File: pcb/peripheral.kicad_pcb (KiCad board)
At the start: 2 copper layers, 37 x 19.6 mm, 0 parts

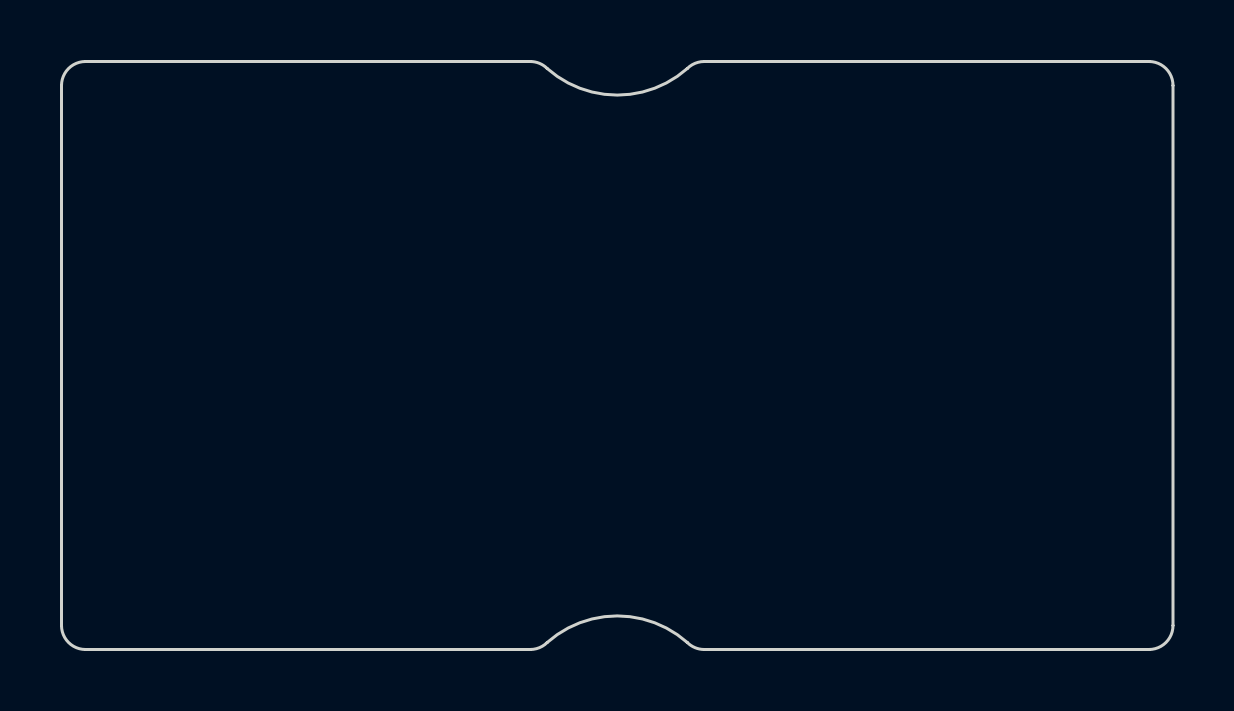
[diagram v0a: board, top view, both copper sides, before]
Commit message: Add Molex connector to peripheral template
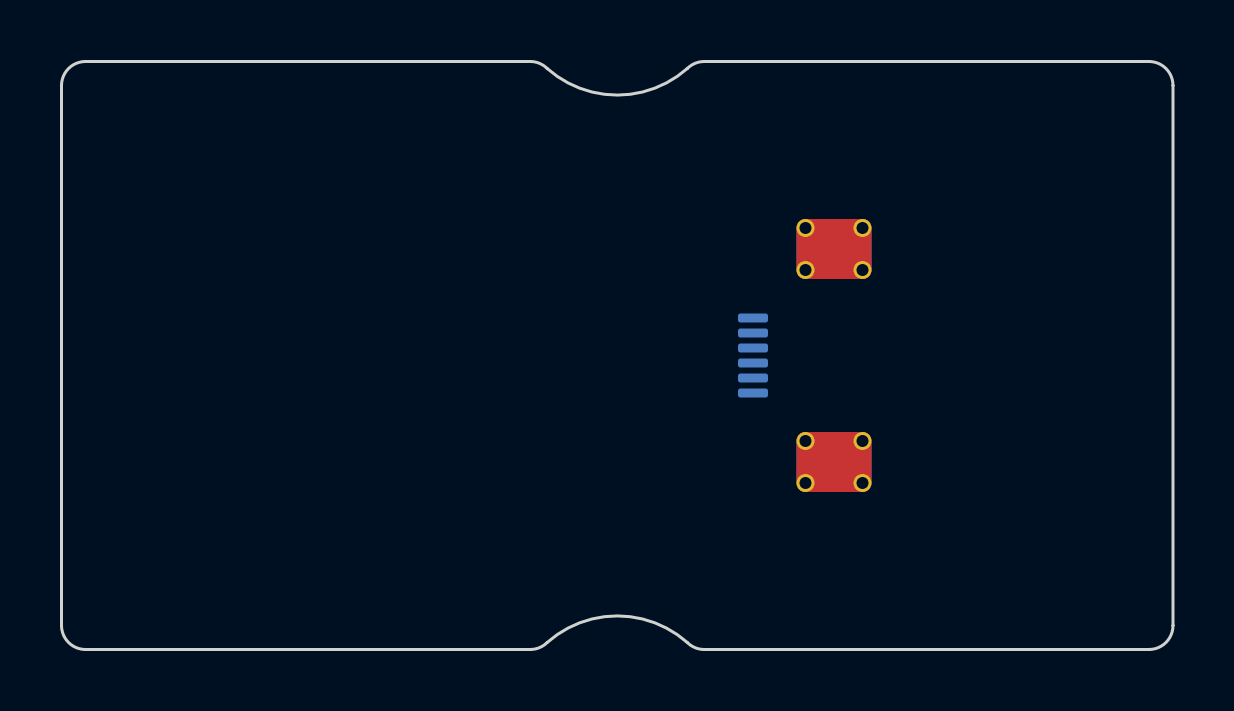
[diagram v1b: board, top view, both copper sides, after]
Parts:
- added J1: Molex-50511, keyboard:Molex_5051100692_1x06_P0.5mm_Anchor_2, B.Cu at (97.0, 100.0)
